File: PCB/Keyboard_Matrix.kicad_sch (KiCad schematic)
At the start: 250 parts, among them J10 Conn_01x01

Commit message: Removing neopixels WIP
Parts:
- removed J10: Conn_01x01, Connector_PinHeader_1.27mm:PinHeader_1x01_P1.27mm_Vertical, symbol Connector_Generic:Conn_01x01
- removed unit 2 of SW1
- removed unit 2 of SW10
- removed unit 2 of SW11
- removed unit 2 of SW12
- removed unit 2 of SW13
- removed unit 2 of SW14
- removed unit 2 of SW15
- removed unit 2 of SW16
- removed unit 2 of SW17
- removed unit 2 of SW18
- removed unit 2 of SW19
- removed unit 2 of SW2
- removed unit 2 of SW20
- removed unit 2 of SW21
- removed unit 2 of SW22
- removed unit 2 of SW23
- removed unit 2 of SW24
- removed unit 2 of SW25
- removed unit 2 of SW26
- removed unit 2 of SW27
- removed unit 2 of SW28
- removed unit 2 of SW29
- removed unit 2 of SW3
- removed unit 2 of SW30
- removed unit 2 of SW31
- removed unit 2 of SW32
- removed unit 2 of SW33
- removed unit 2 of SW34
- removed unit 2 of SW35
- removed unit 2 of SW36
- removed unit 2 of SW37
- removed unit 2 of SW38
- removed unit 2 of SW39
- removed unit 2 of SW4
- removed unit 2 of SW40
- removed unit 2 of SW41
- removed unit 2 of SW42
- removed unit 2 of SW43
- removed unit 2 of SW44
- removed unit 2 of SW45
- removed unit 2 of SW46
- removed unit 2 of SW47
- removed unit 2 of SW48
- removed unit 2 of SW49
- removed unit 2 of SW5
- removed unit 2 of SW50
- removed unit 2 of SW51
- removed unit 2 of SW52
- removed unit 2 of SW53
- removed unit 2 of SW54
- removed unit 2 of SW55
- removed unit 2 of SW56
- removed unit 2 of SW57
- removed unit 2 of SW58
- removed unit 2 of SW59
- removed unit 2 of SW6
- removed unit 2 of SW60
- removed unit 2 of SW61
- removed unit 2 of SW62
- removed unit 2 of SW63
- removed unit 2 of SW64
- removed unit 2 of SW65
- removed unit 2 of SW66
- removed unit 2 of SW67
- removed unit 2 of SW68
- removed unit 2 of SW69
- removed unit 2 of SW7
- removed unit 2 of SW70
- removed unit 2 of SW71
- removed unit 2 of SW72
- removed unit 2 of SW73
- removed unit 2 of SW74
- removed unit 2 of SW75
- removed unit 2 of SW76
- removed unit 2 of SW77
- removed unit 2 of SW78
- removed unit 2 of SW79
- removed unit 2 of SW8
- removed unit 2 of SW80
- removed unit 2 of SW81
- removed unit 2 of SW82
- removed unit 2 of SW83
- removed unit 2 of SW9
- added D100, D102, D103, D104, D105, D106, D107, D108, D109, D110, D111, D112, D113, D114, D115, D116, D117, D118, D119, D120, D121, D122, D123, D124, D125, D126, D127, D128, D129, D130, D131, D132, D133, D134, D135, D136, D137, D138, D139, D140, D141, D142, D143, D144, D145, D146, D147, D148, D149, D150, D151, D152, D153, D154, D155, D156, D157, D158, D159, D160, D161, D162, D163, D164, D165, D166, D167, D168, D169, D170, D171, D172, D86, D87, D88, D89, D90, D91, D92, D93, D94, D95, D96, D97, D98, D99: LED, LED_SMD:LED_1206_3216Metric_ReverseMount_Hole1.8x2.4mm, symbol Device:LED
- added R100, R101, R102, R17, R18, R19, R20, R21, R22, R23, R24, R25, R26, R27, R28, R29, R30, R31, R32, R33, R34, R35, R36, R37, R38, R39, R40, R41, R42, R43, R44, R45, R46, R47, R48, R49, R50, R51, R52, R53, R54, R55, R56, R57, R58, R59, R60, R61, R62, R63, R64, R65, R66, R67, R68, R69, R70, R71, R72, R73, R74, R75, R76, R77, R78, R79, R80, R81, R82, R83, R84, R85, R86, R87, R88, R89, R90, R91, R92, R93, R94, R95, R96, R97, R98, R99: R, Resistor_SMD:R_0603_1608Metric, symbol Device:R
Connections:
- net GND: now also R100.2, R101.2, R102.2, R17.2, R18.2, R19.2, R20.2, R21.2, R22.2, R23.2, R24.2, R25.2, R26.2, R27.2, R28.2, R29.2, R30.2, R31.2, R32.2, R33.2, R34.2, R35.2, R36.2, R37.2, R38.2, R39.2, R40.2, R41.2, R42.2, R43.2, R44.2, R45.2, R46.2, R47.2, R48.2, R49.2, R50.2, R51.2, R52.2, R53.2, R54.2, R55.2, R56.2, R57.2, R58.2, R59.2, R60.2, R61.2, R62.2, R63.2, R64.2, R65.2, R66.2, R67.2, R68.2, R69.2, R70.2, R71.2, R72.2, R73.2, R74.2, R75.2, R76.2, R77.2, R78.2, R79.2, R80.2, R81.2, R82.2, R83.2, R84.2, R85.2, R86.2, R87.2, R88.2, R89.2, R90.2, R91.2, R92.2, R93.2, R94.2, R95.2, R96.2, R97.2, R98.2, R99.2
- net NEOPIX_PWR: now also D100.2 (A), D102.2 (A), D103.2 (A), D104.2 (A), D105.2 (A), D106.2 (A), D107.2 (A), D108.2 (A), D109.2 (A), D110.2 (A), D111.2 (A), D112.2 (A), D113.2 (A), D114.2 (A), D115.2 (A), D116.2 (A), D117.2 (A), D118.2 (A), D119.2 (A), D120.2 (A), D121.2 (A), D122.2 (A), D123.2 (A), D124.2 (A), D125.2 (A), D126.2 (A), D127.2 (A), D128.2 (A), D129.2 (A), D130.2 (A), D131.2 (A), D132.2 (A), D133.2 (A), D134.2 (A), D135.2 (A), D136.2 (A), D137.2 (A), D138.2 (A), D139.2 (A), D140.2 (A), D141.2 (A), D142.2 (A), D143.2 (A), D144.2 (A), D145.2 (A), D146.2 (A), D147.2 (A), D148.2 (A), D149.2 (A), D150.2 (A), D151.2 (A), D152.2 (A), D153.2 (A), D154.2 (A), D155.2 (A), D156.2 (A), D157.2 (A), D158.2 (A), D159.2 (A), D160.2 (A), D161.2 (A), D162.2 (A), D163.2 (A), D164.2 (A), D165.2 (A), D166.2 (A), D167.2 (A), D168.2 (A), D169.2 (A), D170.2 (A), D171.2 (A), D172.2 (A), D86.2 (A), D87.2 (A), D88.2 (A), D89.2 (A), D90.2 (A), D91.2 (A), D92.2 (A), D93.2 (A), D94.2 (A), D95.2 (A), D96.2 (A), D97.2 (A), D98.2 (A), D99.2 (A)
- new net: D120.1 (K), R50.1
- new net: D138.1 (K), R68.1
- new net: D161.1 (K), R91.1
- new net: D139.1 (K), R69.1
- new net: D137.1 (K), R67.1
- new net: D126.1 (K), R56.1
- new net: D141.1 (K), R71.1
- new net: D118.1 (K), R48.1
- new net: D162.1 (K), R92.1
- new net: D107.1 (K), R37.1
- new net: D135.1 (K), R65.1
- new net: D125.1 (K), R55.1
- new net: D129.1 (K), R59.1
- new net: D102.1 (K), R32.1
- new net: D100.1 (K), R31.1
- new net: D158.1 (K), R88.1
- new net: D130.1 (K), R60.1
- new net: D152.1 (K), R82.1
- new net: D169.1 (K), R99.1
- new net: D150.1 (K), R80.1
- new net: D123.1 (K), R53.1
- new net: D97.1 (K), R28.1
- new net: D93.1 (K), R24.1
- new net: D133.1 (K), R63.1
- new net: D114.1 (K), R44.1
- new net: D117.1 (K), R47.1
- new net: D166.1 (K), R96.1
- new net: D98.1 (K), R29.1
- new net: D99.1 (K), R30.1
- new net: D96.1 (K), R27.1
- new net: D140.1 (K), R70.1
- new net: D148.1 (K), R78.1
- new net: D168.1 (K), R98.1
- new net: D122.1 (K), R52.1
- new net: D143.1 (K), R73.1
- new net: D108.1 (K), R38.1
- new net: D86.1 (K), R17.1
- new net: D156.1 (K), R86.1
- new net: D104.1 (K), R34.1
- new net: D115.1 (K), R45.1
- new net: D94.1 (K), R25.1
- new net: D153.1 (K), R83.1
- new net: D128.1 (K), R58.1
- new net: D164.1 (K), R94.1
- new net: D155.1 (K), R85.1
- new net: D146.1 (K), R76.1
- new net: D151.1 (K), R81.1
- new net: D131.1 (K), R61.1
- new net: D87.1 (K), R18.1
- new net: D147.1 (K), R77.1
- new net: D154.1 (K), R84.1
- new net: D105.1 (K), R35.1
- new net: D92.1 (K), R23.1
- new net: D165.1 (K), R95.1
- new net: D103.1 (K), R33.1
- new net: D89.1 (K), R20.1
- new net: D149.1 (K), R79.1
- new net: D145.1 (K), R75.1
- new net: D113.1 (K), R43.1
- new net: D88.1 (K), R19.1
- new net: D127.1 (K), R57.1
- new net: D106.1 (K), R36.1
- new net: D160.1 (K), R90.1
- new net: D91.1 (K), R22.1
- new net: D109.1 (K), R39.1
- new net: D111.1 (K), R41.1
- new net: D134.1 (K), R64.1
- new net: D142.1 (K), R72.1
- new net: D132.1 (K), R62.1
- new net: D157.1 (K), R87.1
- new net: D121.1 (K), R51.1
- new net: D163.1 (K), R93.1
- new net: D172.1 (K), R102.1
- new net: D136.1 (K), R66.1
- new net: D159.1 (K), R89.1
- new net: D90.1 (K), R21.1
- new net: D171.1 (K), R101.1
- new net: D170.1 (K), R100.1
- new net: D167.1 (K), R97.1
- new net: D119.1 (K), R49.1
- new net: D112.1 (K), R42.1
- new net: D144.1 (K), R74.1
- new net: D124.1 (K), R54.1
- new net: D95.1 (K), R26.1
- new net: D116.1 (K), R46.1
- new net: D110.1 (K), R40.1

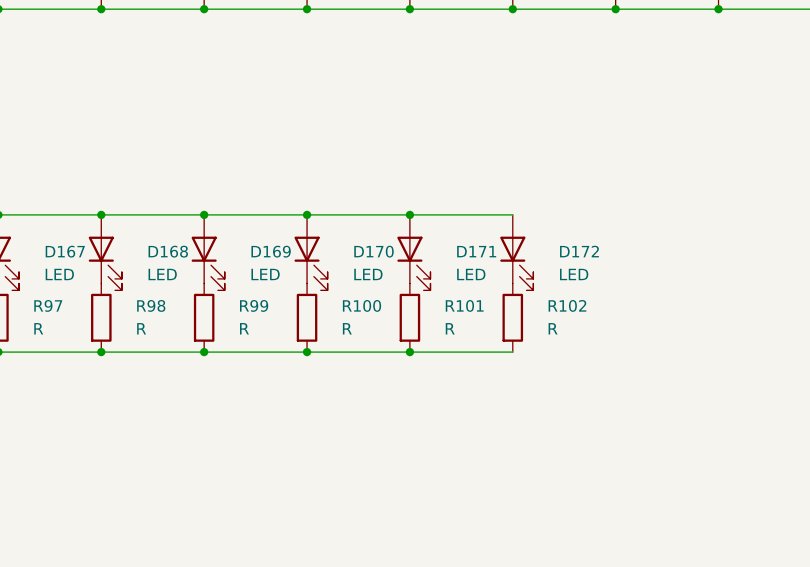
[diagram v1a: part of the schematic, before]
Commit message: add white leds
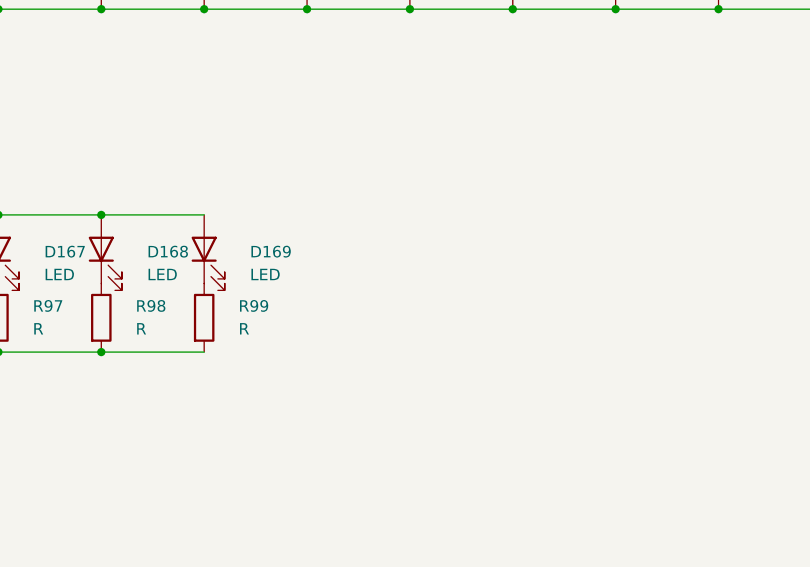
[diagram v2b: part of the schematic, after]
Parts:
- removed D170, D171, D172: LED, LED_SMD:LED_1206_3216Metric_ReverseMount_Hole1.8x2.4mm, symbol Device:LED
- removed R100, R101, R102: R, Resistor_SMD:R_0603_1608Metric, symbol Device:R

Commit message: Changed battery managment IC and LDO
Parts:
- removed C11, C12, C13, C14, C15, C16, C17, C18, C19, C20, C21, C22, C23, C24, C25, C26, C27, C28, C29, C30, C31, C32, C33, C34, C35, C36, C37, C38, C39, C40, C41, C42, C43, C44, C45, C46, C47, C48, C49, C50, C51, C52, C53, C54, C55, C56, C57, C58, C59, C60, C61, C62, C63, C64, C65, C66, C67, C68, C69, C70, C71, C72, C73, C74, C75, C76, C77, C78, C79, C80, C81, C82, C83, C84, C85, C86, C87, C88, C89, C90, C91, C92, C93: 100n, Capacitor_SMD:C_0603_1608Metric, symbol Device:C
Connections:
- removed net GND: R17.2, R18.2, R19.2, R20.2, R21.2, R22.2, R23.2, R24.2, R25.2, R26.2, R27.2, R28.2, R29.2, R30.2, R31.2, R32.2, R33.2, R34.2, R35.2, R36.2, R37.2, R38.2, R39.2, R40.2, R41.2, R42.2, R43.2, R44.2, R45.2, R46.2, R47.2, R48.2, R49.2, R50.2, R51.2, R52.2, R53.2, R54.2, R55.2, R56.2, R57.2, R58.2, R59.2, R60.2, R61.2, R62.2, R63.2, R64.2, R65.2, R66.2, R67.2, R68.2, R69.2, R70.2, R71.2, R72.2, R73.2, R74.2, R75.2, R76.2, R77.2, R78.2, R79.2, R80.2, R81.2, R82.2, R83.2, R84.2, R85.2, R86.2, R87.2, R88.2, R89.2, R90.2, R91.2, R92.2, R93.2, R94.2, R95.2, R96.2, R97.2, R98.2, R99.2
- net NEOPIX_PWR renamed V_Raw
- new net BL_R0: R17.2, R18.2, R19.2, R20.2, R21.2, R22.2, R23.2, R24.2, R25.2, R26.2, R27.2, R28.2, R29.2, R30.2, R31.2
- new net BL_R1: R32.2, R33.2, R34.2, R35.2, R36.2, R37.2, R38.2, R39.2, R40.2, R41.2, R42.2, R43.2, R44.2, R45.2, R46.2, R47.2
- new net BL_R2: R48.2, R49.2, R50.2, R51.2, R52.2, R53.2, R54.2, R55.2, R56.2, R57.2, R58.2, R59.2, R60.2, R61.2, R62.2, R63.2
- new net BL_R3: R64.2, R65.2, R66.2, R67.2, R68.2, R69.2, R70.2, R71.2, R72.2, R73.2, R74.2, R75.2, R76.2
- new net BL_R4: R77.2, R78.2, R79.2, R80.2, R81.2, R82.2, R83.2, R84.2, R85.2, R86.2, R87.2, R88.2, R89.2
- new net BL_R5: R90.2, R91.2, R92.2, R93.2, R94.2, R95.2, R96.2, R97.2, R98.2, R99.2
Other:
- moved on the sheet: D100, D102, D103, D104, D105, D106, D107, D108, D109, D110, D111, D112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

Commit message: Add boost regulator for LEDs
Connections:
- net V_Raw renamed +5V

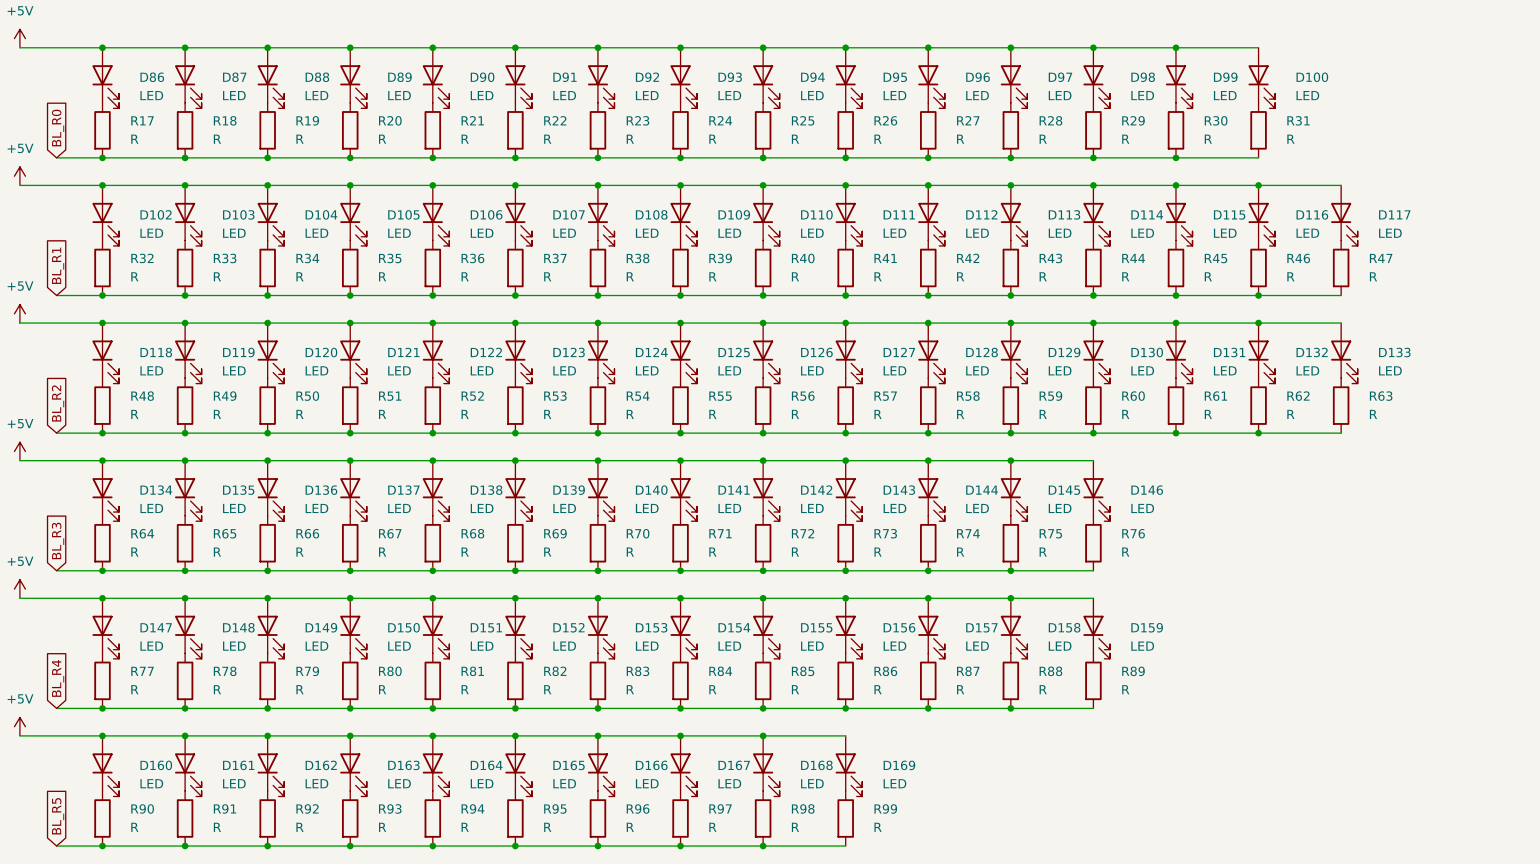
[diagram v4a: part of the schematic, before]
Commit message: Update LED resistor value
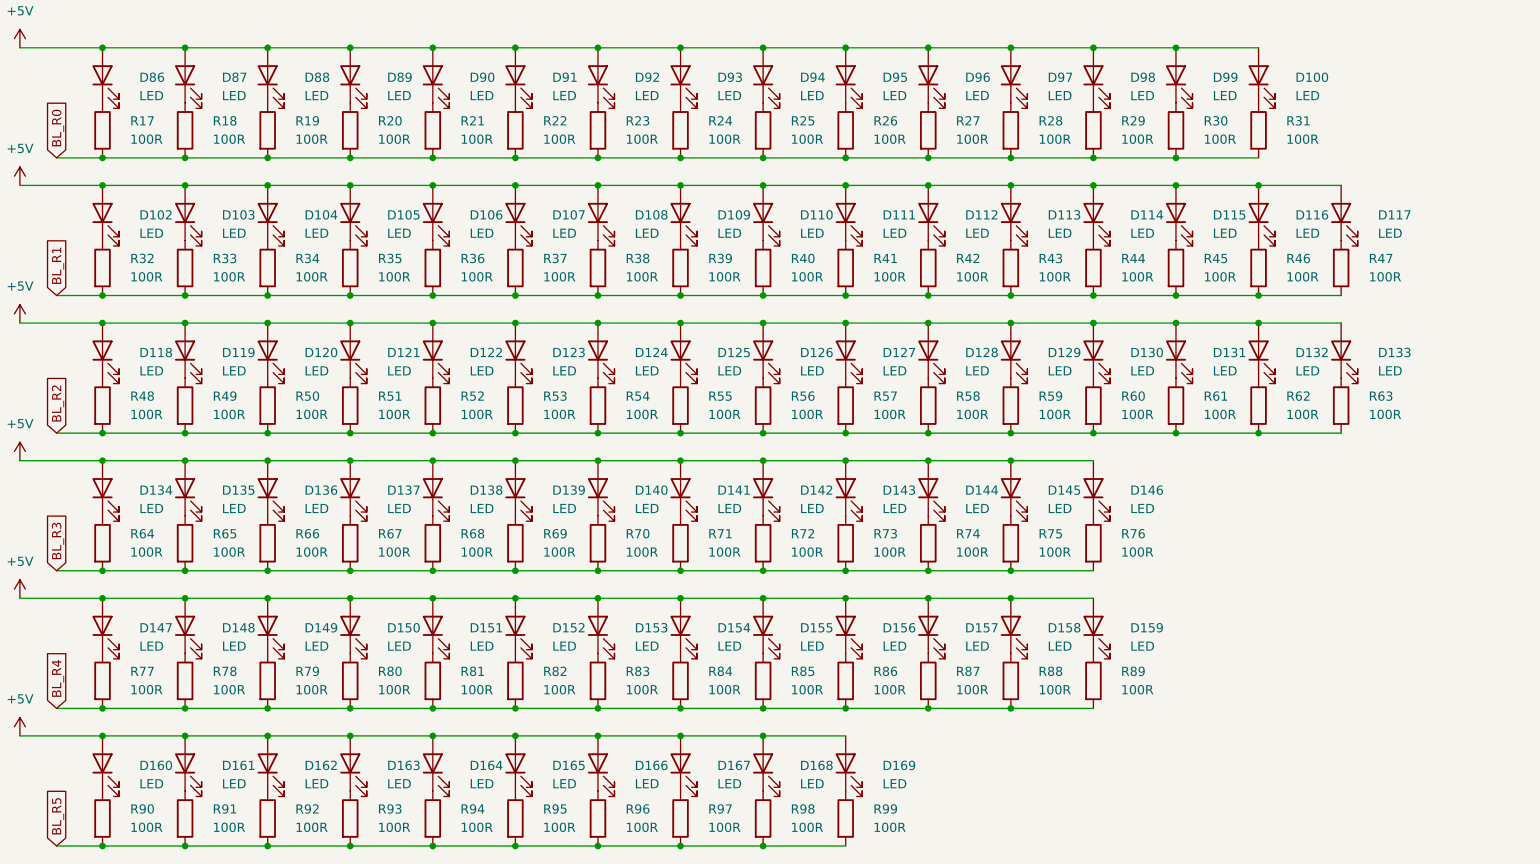
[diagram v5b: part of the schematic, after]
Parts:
- R17, R18, R19, R20, R21, R22, R23, R24, R25, R26, R27, R28, R29, R30, R31, R32, R33, R34, R35, R36, R37, R38, R39, R40, R41, R42, R43, R44, R45, R46, R47, R48, R49, R50, R51, R52, R53, R54, R55, R56, R57, R58, R59, R60, R61, R62, R63, R64, R65, R66, R67, R68, R69, R70, R71, R72, R73, R74, R75, R76, R77, R78, R79, R80, R81, R82, R83, R84, R85, R86, R87, R88, R89, R90, R91, R92, R93, R94, R95, R96, R97, R98, R99: value R -> 100R
